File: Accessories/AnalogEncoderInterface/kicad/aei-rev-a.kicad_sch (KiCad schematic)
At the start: 34 parts, among them J1 Screw_Terminal_01x06, J2 1935161, U1 INA2143U, U2 INA2143U, U3 LT1764EQ-1.5-PBF, U4 RJHSE5380

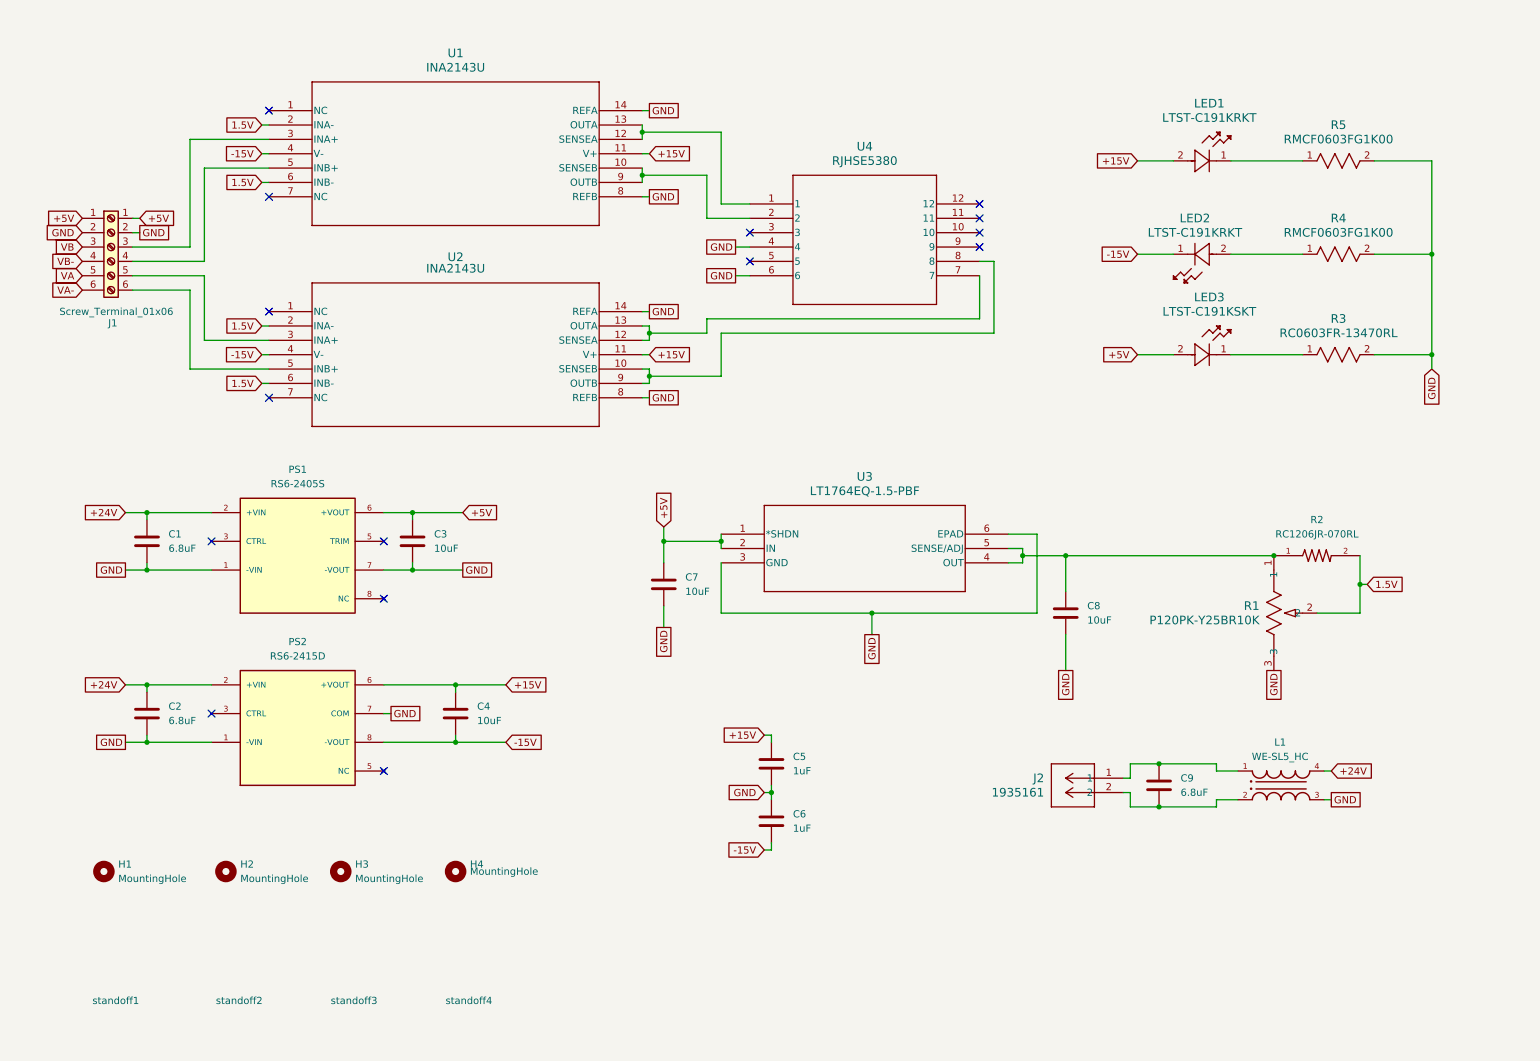
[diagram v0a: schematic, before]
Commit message: Update schematic with GND_24V, isolation, and test points
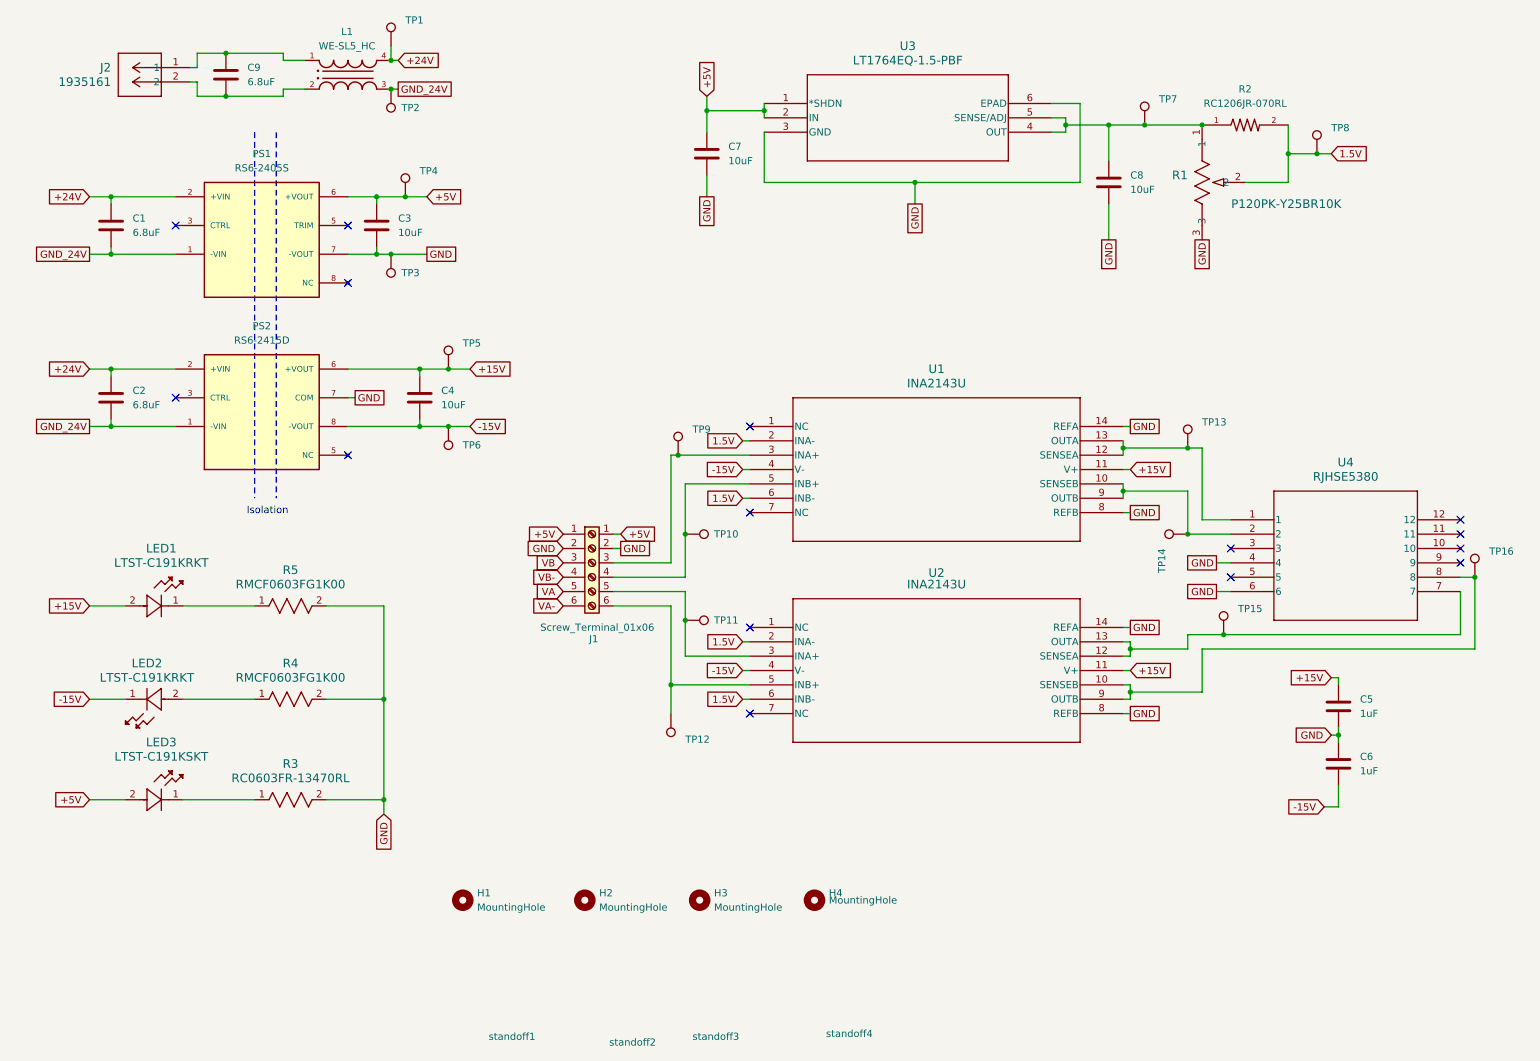
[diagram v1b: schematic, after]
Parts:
- added TP1, TP10, TP11, TP12, TP13, TP14, TP15, TP16, TP2, TP3, TP4, TP5, TP6, TP7, TP8, TP9: TestPoint, symbol Connector:TestPoint
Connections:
- net +15V: now also TP5.1
- net +24V: now also TP1.1
- net +5V: now also TP4.1
- net -15V: now also TP6.1
- net 1.5V: now also TP8.1
- net GND: now also TP3.1; no longer C1.2, C2.2, L1.3, PS1.1 (-VIN), PS2.1 (-VIN)
- net at U2.10 (SENSEB), U2.9 (OUTB), U4.8: now also TP16.1
- net at U2.12 (SENSEA), U2.13 (OUTA), U4.7: now also TP15.1
- net at J1.5, U2.3 (INA+): now also TP11.1
- net at J1.6, U2.5 (INB+): now also TP12.1
- net at C8.1, R1.1, R2.1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: now also TP7.1
- net at U1.12 (SENSEA), U1.13 (OUTA), U4.1: now also TP13.1
- net at U1.10 (SENSEB), U1.9 (OUTB), U4.2: now also TP14.1
- net at J1.3, U1.3 (INA+): now also TP9.1
- net at J1.4, U1.5 (INB+): now also TP10.1
- new net GND_24V: C1.2, C2.2, L1.3, PS1.1 (-VIN), PS2.1 (-VIN), TP2.1
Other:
- note added: "Isolation"
- company: AMDC Rotary Position -> AMDC- Hardware
- title: Buffer Circuit - Breadboard -> Analog Encoder Interfacing Circuit
- moved on the sheet: C1, C2, C3, C4, C5, C6, C7, C8, C9, H1, H2, H3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

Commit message: Add footprint sizes
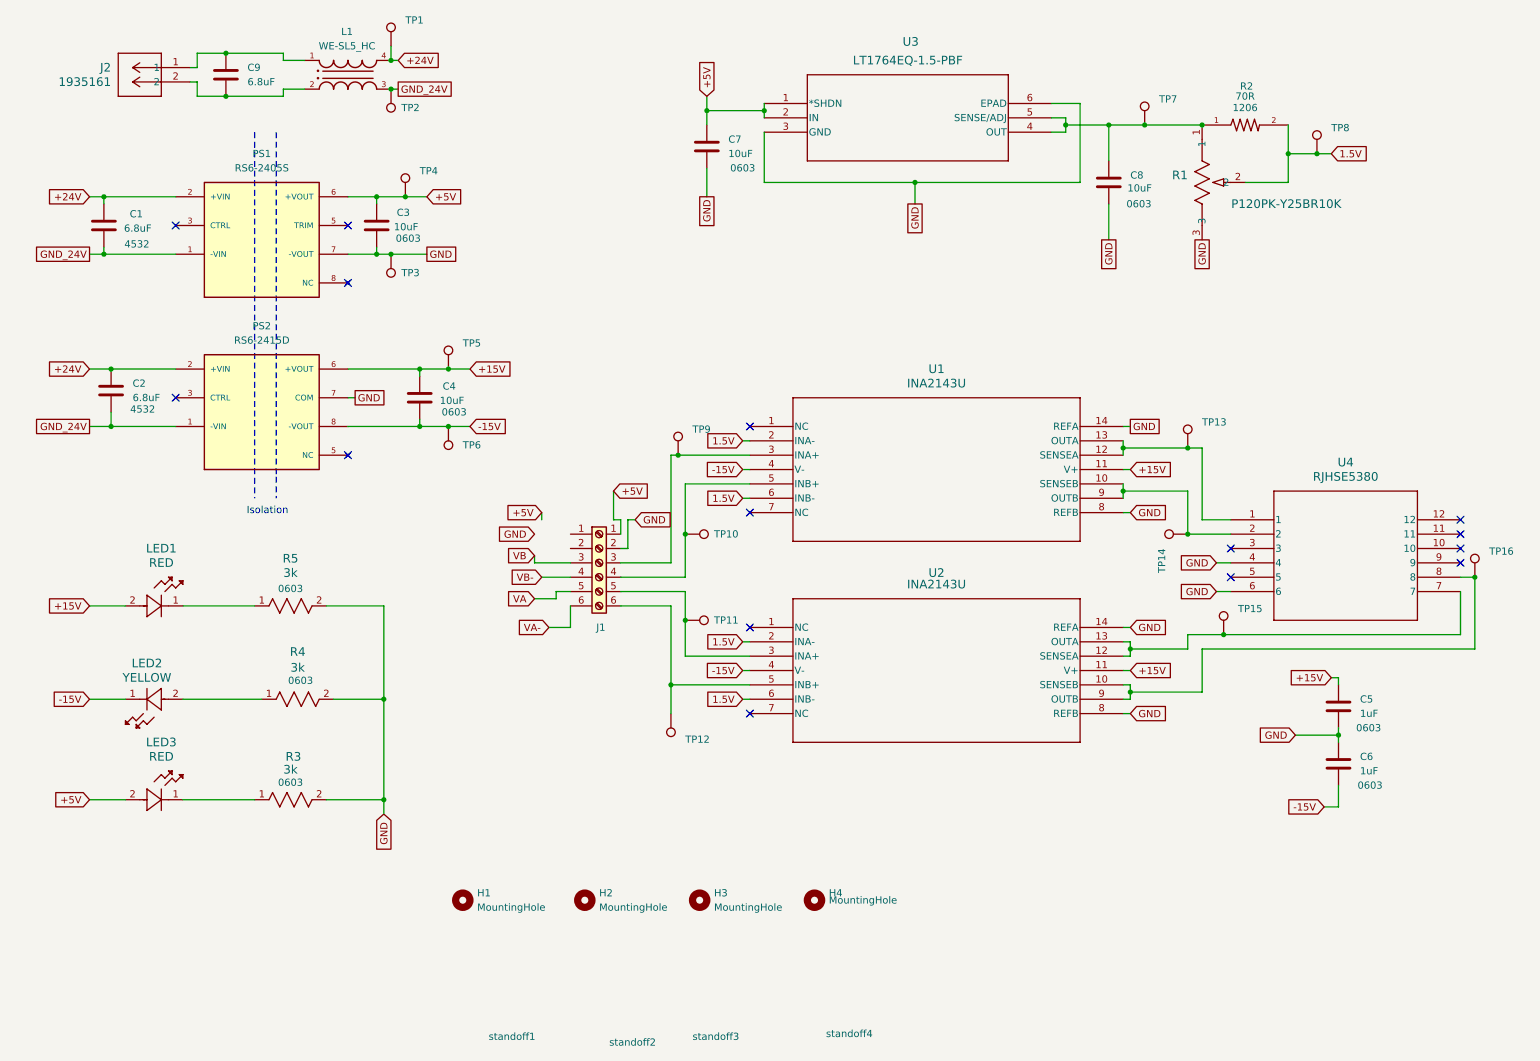
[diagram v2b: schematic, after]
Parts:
- LED1: value LTST-C191KRKT -> RED
- LED2: value LTST-C191KRKT -> YELLOW
- LED3: value LTST-C191KSKT -> RED
- R2: value RC1206JR-070RL -> 70R
- R3: value RC0603FR-13470RL -> 3k
- R4, R5: value RMCF0603FG1K00 -> 3k
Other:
- moved on the sheet: C1, C2, C7, J1, R4

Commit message: Update schematic and add screw connector for MTS drive
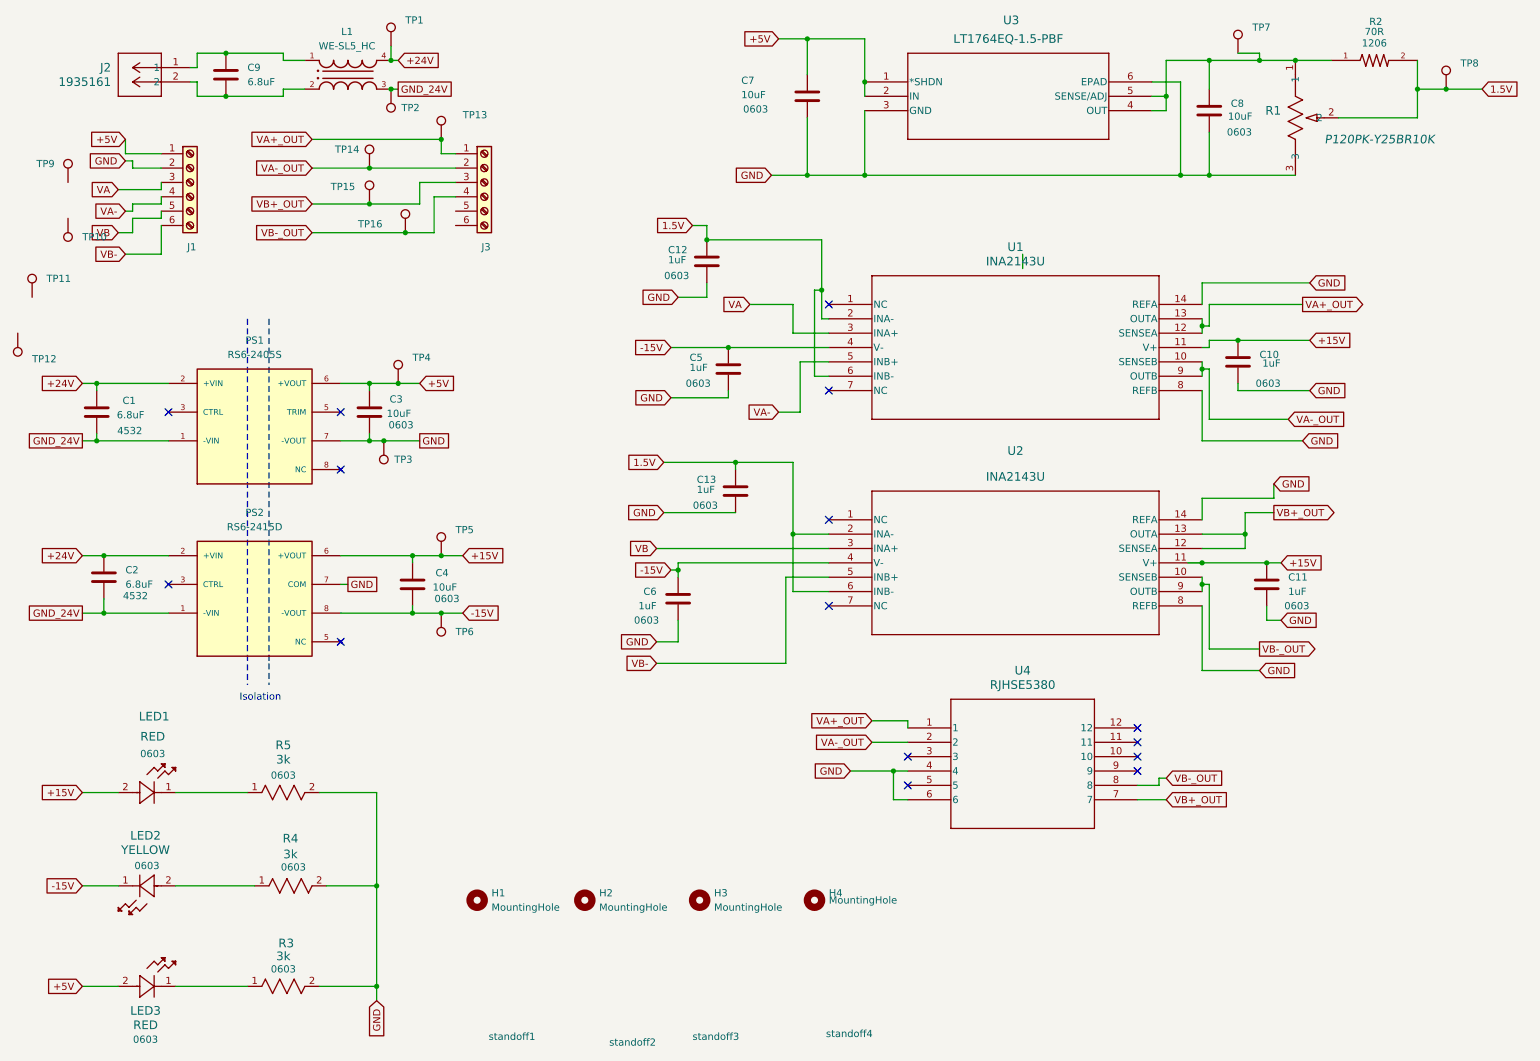
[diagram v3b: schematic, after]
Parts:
- added C10, C11, C12, C13: 1uF, Capacitor_SMD:C_0201_0603Metric, symbol Device:C
- added J3: Screw_Terminal_01x06, TerminalBlock_Phoenix:TerminalBlock_Phoenix_MKDS-1,5-6_1x06_P5.00mm_Horizontal, symbol Connector:Screw_Terminal_01x06
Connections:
- net +15V: now also C10.1, C11.1; no longer C5.1
- net -15V: now also C5.1, C6.1; no longer C6.2
- net 1.5V: now also C12.1, C13.1
- net GND: now also C6.2, C10.2, C11.2, C12.2, C13.2; no longer C6.1
- net VA: now also J1.3 (Pin_3), U1.3 (INA+); no longer J1.5
- net VA-: now also J1.4 (Pin_4), U1.5 (INB+); no longer J1.6
- net VB: now also J1.5 (Pin_5), U2.3 (INA+); no longer J1.3
- net VB-: now also J1.6 (Pin_6), U2.5 (INB+); no longer J1.4
- net VB-_OUT: now reaches TP16.1, U2.10 (SENSEB), U2.9 (OUTB), U4.8
- net VB-_OUT: now also J3.4 (Pin_4)
- net VB+_OUT: now reaches TP15.1, U2.12 (SENSEA), U2.13 (OUTA), U4.7
- net VB+_OUT: now also J3.3 (Pin_3)
- net VA-_OUT: now reaches TP14.1, U1.10 (SENSEB), U1.9 (OUTB), U4.2
- net VA-_OUT: now also J3.2 (Pin_2)
- net VA+_OUT: now reaches TP13.1, U1.12 (SENSEA), U1.13 (OUTA), U4.1
- net VA+_OUT: now also J3.1 (Pin_1)
- now unconnected: TP10.1, TP11.1, TP12.1, TP9.1
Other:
- moved on the sheet: C1, C2, C3, C4, C5, C6, C7, C8, H1, LED1, LED2, LED3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

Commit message: update the schematics
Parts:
- removed U4: RJHSE5380, RJHSE5380:RJHSE5380_AMP, symbol RJHSE5380:RJHSE5380
- added J4: RJ45, symbol Connector:RJ45
- added TP17, TP18, TP19: TestPoint, symbol Connector:TestPoint
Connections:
- net +5V: now also TP9.1
- net GND: now also J3.5 (Pin_5), TP10.1, J4.4, J4.6, TP17.1
- net VA: now also TP11.1
- net VA+_OUT: now also J4.1
- net VA-: now also TP12.1
- net VA-_OUT: now also J4.2
- net VB: now also TP18.1
- net VB+_OUT: now also J4.7
- net VB-: now also TP19.1
- net VB-_OUT: now also J4.8
- no-connect marks 15 -> 12
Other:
- moved on the sheet: J1, J3, TP10, TP11, TP12, TP13, TP14, TP15, TP16, TP9
